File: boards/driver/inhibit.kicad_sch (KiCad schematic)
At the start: 11 parts, among them Q1 MMBT2222, Q2 MMBT2222

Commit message: Driver: filled out the rest of the BOM, except for defaults for nominal resistances
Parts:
- R1: MPN (none) -> ESR03EZPF1001; Manufacturer (none) -> Rohm Semiconductor; Package (none) -> 0603; Rating (none) -> 1/4W; Tolerance (none) -> 1%
- R2: MPN (none) -> ERJ-PA3F3900V; Manufacturer (none) -> Panasonic Electronic Components; Package (none) -> 0603; Rating (none) -> 1/3W; Tolerance (none) -> 1%
- R3: MPN (none) -> CRCW06034R70FKEAHP; Manufacturer (none) -> Vishay Dale; Package (none) -> 0603; Rating (none) -> 1/3W; Tolerance (none) -> 1%
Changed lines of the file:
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@@
+      (effects (font (size 1.27 1.27)) hide)
+    )
+    (property "Description" "RES SMD 1K OHM PULSE-WITHSTANDING 1% 1/4W 0603" (id 4) (at 92.71 90.17 0)
+      (effects (font (size 1.27 1.27)) hide)
+    )
+    (property "MPN" "ESR03EZPF1001" (id 5) (at 92.71 90.17 0)
+      (effects (font (size 1.27 1.27)) hide)
+    )
+    (property "Manufacturer" "Rohm Semiconductor" (id 6) (at 92.71 90.17 0)
+      (effects (font (size 1.27 1.27)) hide)
+    )
+    (property "Package" "0603" (id 7) (at 92.71 90.17 0)
+      (effects (font (size 1.27 1.27)) hide)
+    )
+    (property "Rating" "1/4W" (id 8) (at 92.71 90.17 0)
+      (effects (font (size 1.27 1.27)) hide)
+    )
+    (property "Tolerance" "1%" (id 9) (at 92.71 90.17 0)
       (effects (font (size 1.27 1.27)) hide)
     )
@@
       (effects (font (size 1.27 1.27)) hide)
     )
+    (property "Description" "RES SMD 4.7 OHM PULSE-WITHSTANDING 1% 1/3W 0603" (id 4) (at 135.89 91.44 0)
+      (effects (font (size 1.27 1.27)) hide)
+    )
+    (property "MPN" "CRCW06034R70FKEAHP" (id 5) (at 135.89 91.44 0)
+      (effects (font (size 1.27 1.27)) hide)
+    )
+    (property "Manufacturer" "Vishay Dale" (id 6) (at 135.89 91.44 0)
+      (effects (font (size 1.27 1.27)) hide)
+    )
+    (property "Package" "0603" (id 7) (at 135.89 91.44 0)
+      (effects (font (size 1.27 1.27)) hide)
+    )
+    (property "Rating" "1/3W" (id 8) (at 135.89 91.44 0)
+      (effects (font (size 1.27 1.27)) hide)
+    )
+    (property "Tolerance" "1%" (id 9) (at 135.89 91.44 0)
+      (effects (font (size 1.27 1.27)) hide)
+    )
     (pin "1")
     (pin "2")
@@
       (effects (font (size 1.27 1.27)) hide)
     )
+    (property "Description" "RES SMD 390 OHM PULSE-WITHSTANDING 1% 1/3W 0603" (id 4) (at 106.68 74.93 0)
+      (effects (font (size 1.27 1.27)) hide)
+    )
+    (property "MPN" "ERJ-PA3F3900V" (id 5) (at 106.68 74.93 0)
+      (effects (font (size 1.27 1.27)) hide)
+    )
+    (property "Manufacturer" "Panasonic Electronic Components" (id 6) (at 106.68 74.93 0)
+      (effects (font (size 1.27 1.27)) hide)
+    )
+    (property "Package" "0603" (id 7) (at 106.68 74.93 0)
+      (effects (font (size 1.27 1.27)) hide)
+    )
+    (property "Rating" "1/3W" (id 8) (at 106.68 74.93 0)
+      (effects (font (size 1.27 1.27)) hide)
+    )
+    (property "Tolerance" "1%" (id 9) (at 106.68 74.93 0)
+      (effects (font (size 1.27 1.27)) hide)
+    )

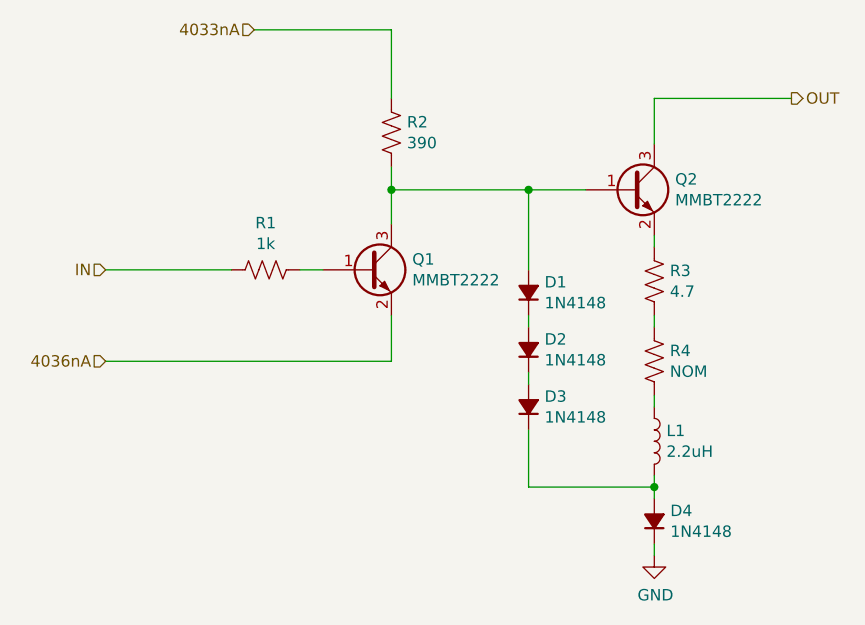
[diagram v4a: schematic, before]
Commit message: Driver: completed the BOM and added some reference dimensions to the board layout
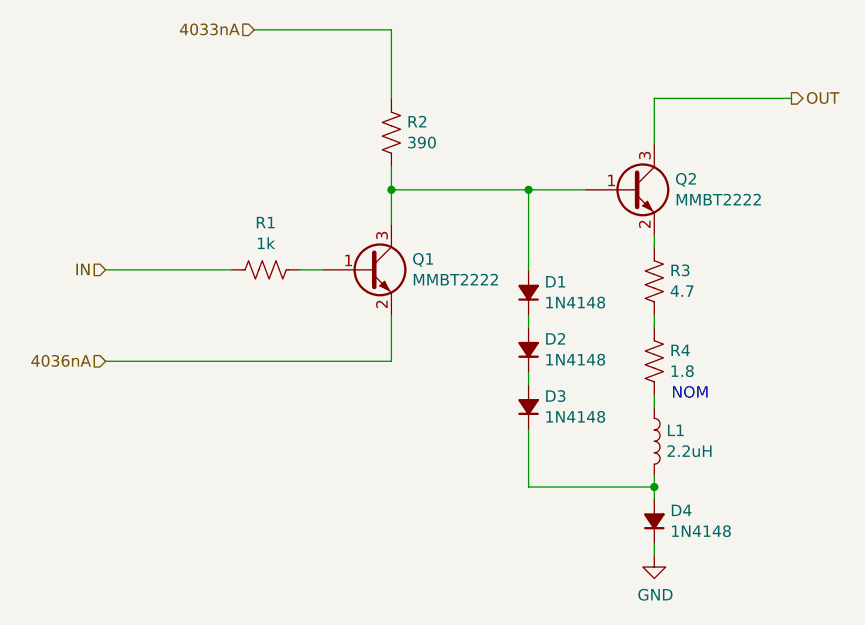
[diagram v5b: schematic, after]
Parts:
- R4: value NOM -> 1.8; MPN (none) -> SDR03EZPF1R80; Manufacturer (none) -> Rohm Semiconductor; Package (none) -> 0603; Rating (none) -> 0.3W; Tolerance (none) -> 1%
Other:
- note added: "NOM"
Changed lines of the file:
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@@
     (stroke (width 0) (type default) (color 0 0 0 0))
+  )
+  (text "NOM" (at 137.795 104.775 0)
+    (effects (font (size 1.27 1.27)) (justify left bottom))
   )
   (hierarchical_label "IN" (shape input) (at 74.93 90.17 180)
@@
       (effects (font (size 1.27 1.27)) (justify left))
     )
-    (property "Value" "NOM" (id 1) (at 137.6172 101.473 0)
+    (property "Value" "1.8" (id 1) (at 137.6172 101.473 0)
       (effects (font (size 1.27 1.27)) (justify left))
     )
@@
       (effects (font (size 1.27 1.27)) hide)
     )
+    (property "Description" "RES SMD 1.8 OHM PULSE-WITHSTANDING 1% 0.3W 0603" (id 4) (at 135.89 100.33 0)
+      (effects (font (size 1.27 1.27)) hide)
+    )
+    (property "MPN" "SDR03EZPF1R80" (id 5) (at 135.89 100.33 0)
+      (effects (font (size 1.27 1.27)) hide)
+    )
+    (property "Manufacturer" "Rohm Semiconductor" (id 6) (at 135.89 100.33 0)
+      (effects (font (size 1.27 1.27)) hide)
+    )
+    (property "Package" "0603" (id 7) (at 135.89 100.33 0)
+      (effects (font (size 1.27 1.27)) hide)
+    )
+    (property "Rating" "0.3W" (id 8) (at 135.89 100.33 0)
+      (effects (font (size 1.27 1.27)) hide)
+    )
+    (property "Tolerance" "1%" (id 9) (at 135.89 100.33 0)
+      (effects (font (size 1.27 1.27)) hide)
+    )
